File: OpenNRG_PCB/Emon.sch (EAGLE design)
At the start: 63 parts, among them J1 POWER_JACKSMD, Q4 16000, U1 ATMEGA368

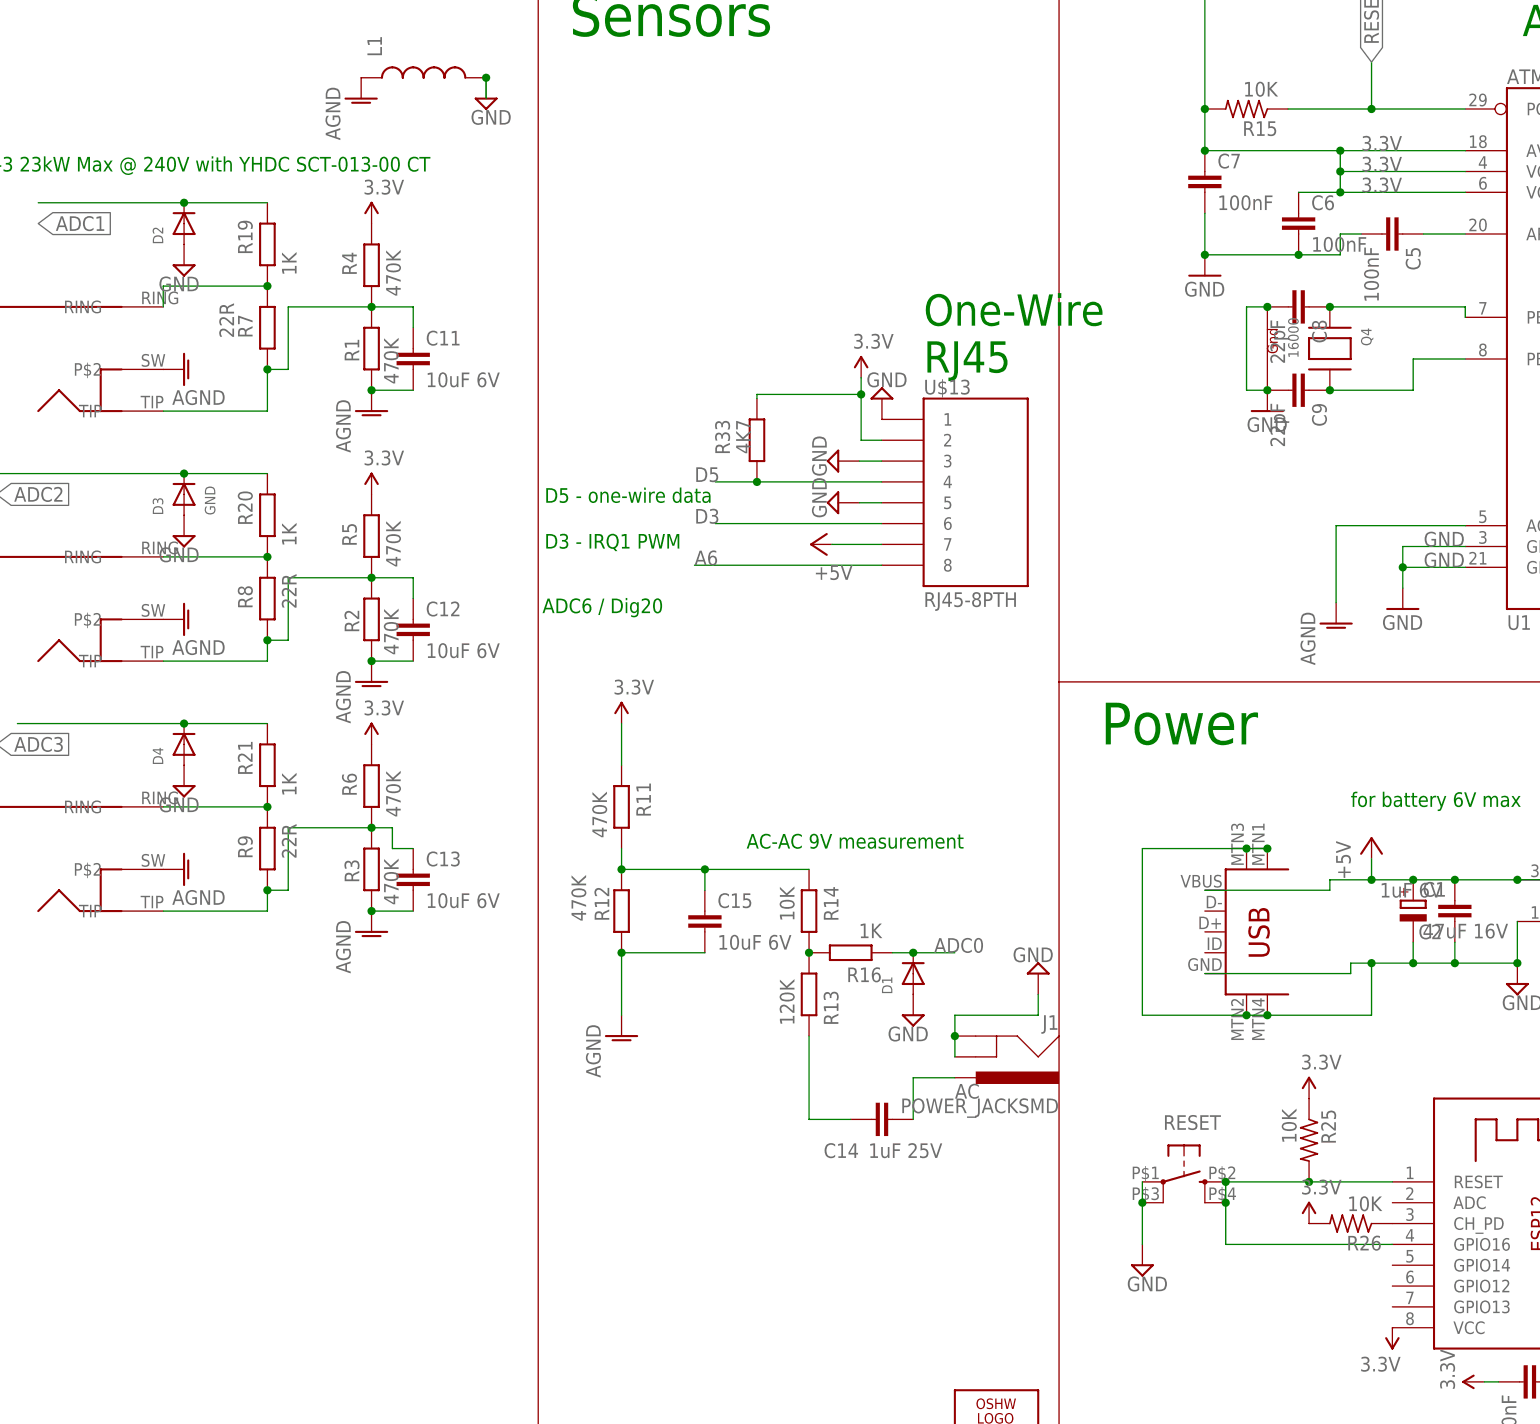
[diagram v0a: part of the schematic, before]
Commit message: Re-write or ESP code and updated to board files
Update to ESP8266 firmware to support latest board manager.
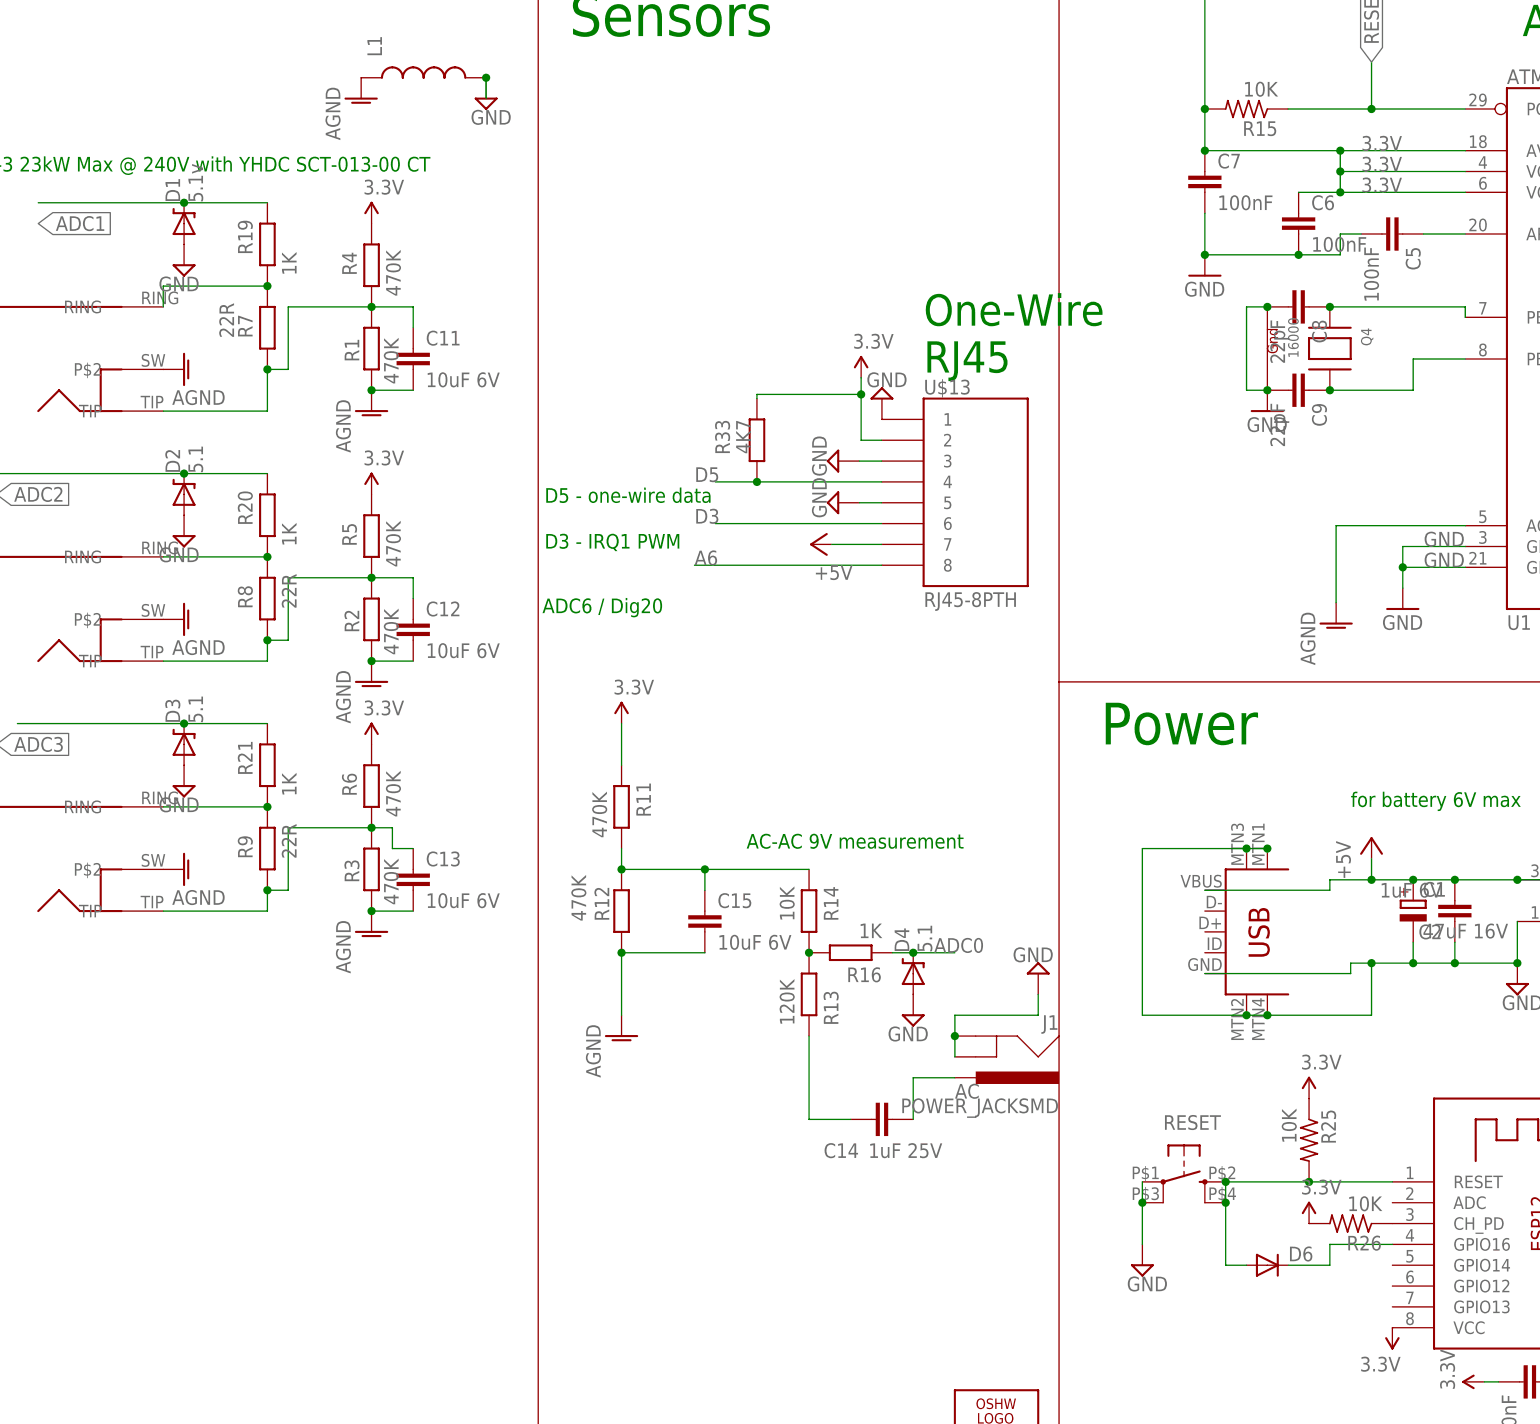
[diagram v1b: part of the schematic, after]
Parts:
- added D6: (no value), SparkFun:DIODESOD
- D1: value (none) -> 5.1v; device microbuilder:DIODESOD-523 -> SparkFun:DIODE-ZENER-BZT52
- D2, D4: value (none) -> 5.1; device microbuilder:DIODESOD-523 -> SparkFun:DIODE-ZENER-BZT52
- D3: value GND -> 5.1; device microbuilder:DIODESOD-523 -> SparkFun:DIODE-ZENER-BZT52
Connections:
- new net N$12: D6.C, X1.GPIO16
- net ADC0: now also D4.C; no longer D1.C
- net ADC1: now also D1.C; no longer D2.C
- net ADC2: now also D2.C; no longer D3.C
- net ADC3: now also D3.C; no longer D4.C
- net N$15: now also D6.A; no longer X1.GPIO16
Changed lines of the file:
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@@
 <part name="P+9" library="supply1" deviceset="+5V" device=""/>
 <part name="AGND11" library="supply1" deviceset="AGND" device=""/>
-<part name="D2" library="microbuilder" deviceset="DIODE" device="SOD-523"/>
-<part name="D3" library="microbuilder" deviceset="DIODE" device="SOD-523" value="GND"/>
-<part name="D4" library="microbuilder" deviceset="DIODE" device="SOD-523"/>
 <part name="SUPPLY14" library="supply2" deviceset="GND" device=""/>
 <part name="SUPPLY16" library="supply2" deviceset="GND" device=""/>
 <part name="SUPPLY17" library="supply2" deviceset="GND" device=""/>
-<part name="D1" library="microbuilder" deviceset="DIODE" device="SOD-523"/>
 <part name="SUPPLY18" library="supply2" deviceset="GND" device=""/>
 <part name="P+2" library="supply1" deviceset="+5V" device=""/>
@@
 <part name="U$3" library="Qxd" deviceset="MJ-3523-SMT" device=""/>
 <part name="J1" library="SparkFun" deviceset="POWER_JACK" device="SMD"/>
-<part name="U$4" library="Qxd" deviceset="AUDIO_SMT" device=""/>
+<part name="D1" library="SparkFun" deviceset="DIODE-ZENER" device="-BZT52" value="5.1v"/>
+<part name="D2" library="SparkFun" deviceset="DIODE-ZENER" device="-BZT52" value="5.1"/>
+<part name="D3" library="SparkFun" deviceset="DIODE-ZENER" device="-BZT52" value="5.1"/>
+<part name="D4" library="SparkFun" deviceset="DIODE-ZENER" device="-BZT52" value="5.1"/>
+<part name="D6" library="SparkFun" deviceset="DIODE" device="SOD"/>
 </parts>
 <sheets>
@@
 <instance part="P+9" gate="1" x="7.874" y="308.864" rot="R90"/>
 <instance part="AGND11" gate="VR1" x="71.882" y="299.212"/>
-<instance part="D2" gate="G$1" x="-68.58" y="347.98" rot="R90"/>
-<instance part="D3" gate="G$1" x="-68.58" y="314.96" rot="R90"/>
-<instance part="D4" gate="G$1" x="-68.58" y="284.48" rot="R90"/>
 <instance part="SUPPLY14" gate="GND" x="-68.58" y="279.4" rot="MR0"/>
 <instance part="SUPPLY16" gate="GND" x="-68.58" y="342.9" rot="MR0"/>
 <instance part="SUPPLY17" gate="GND" x="-68.58" y="309.88" rot="MR0"/>
-<instance part="D1" gate="G$1" x="20.32" y="256.54" rot="R90"/>
 <instance part="SUPPLY18" gate="GND" x="20.32" y="251.46" rot="MR0"/>
 <instance part="P+2" gate="1" x="256.54" y="321.31"/>
@@
 <instance part="U$3" gate="G$1" x="-86.36" y="271.78"/>
 <instance part="J1" gate="G$1" x="27.94" y="251.46" rot="R180"/>
+<instance part="D1" gate="G$1" x="-68.58" y="347.98" rot="R90"/>
+<instance part="D2" gate="G$1" x="-68.58" y="314.96" rot="R90"/>
+<instance part="D3" gate="G$1" x="-68.58" y="284.48" rot="R90"/>
+<instance part="D4" gate="G$1" x="20.32" y="256.54" rot="R90"/>
+<instance part="D6" gate="G$1" x="63.5" y="220.98"/>
 </instances>
 <busses>
@@
 </segment>
 <segment>
-<pinref part="D4" gate="G$1" pin="A"/>
-<pinref part="SUPPLY14" gate="GND" pin="GND"/>
-</segment>
-<segment>
-<pinref part="D2" gate="G$1" pin="A"/>
-<pinref part="SUPPLY16" gate="GND" pin="GND"/>
-</segment>
-<segment>
-<pinref part="D3" gate="G$1" pin="A"/>
-<pinref part="SUPPLY17" gate="GND" pin="GND"/>
-</segment>
-<segment>
-<pinref part="D1" gate="G$1" pin="A"/>
-<pinref part="SUPPLY18" gate="GND" pin="GND"/>
-</segment>
-<segment>
 <pinref part="X1" gate="G$1" pin="GND"/>
 <pinref part="SUPPLY4" gate="GND" pin="GND"/>
@@
 <wire x1="218.44" y1="261.62" x2="226.06" y2="261.62" width="0.1524" layer="91"/>
 </segment>
+<segment>
+<pinref part="SUPPLY16" gate="GND" pin="GND"/>
+<pinref part="D1" gate="G$1" pin="A"/>
+</segment>
+<segment>
+<pinref part="SUPPLY17" gate="GND" pin="GND"/>
+<pinref part="D2" gate="G$1" pin="A"/>
+</segment>
+<segment>
+<pinref part="SUPPLY14" gate="GND" pin="GND"/>
+<pinref part="D3" gate="G$1" pin="A"/>
+</segment>
+<segment>
+<pinref part="SUPPLY18" gate="GND" pin="GND"/>
+<pinref part="D4" gate="G$1" pin="A"/>
+</segment>
 </net>
 <net name="ADC0" class="0">
 <segment>
 <pinref part="R16" gate="G$1" pin="1"/>
+<label x="22.86" y="259.08" size="1.778" layer="95"/>
 <wire x1="17.78" y1="259.08" x2="20.32" y2="259.08" width="0.1524" layer="91"/>
-<label x="22.86" y="259.08" size="1.778" layer="95"/>
-<pinref part="D1" gate="G$1" pin="C"/>
+<pinref part="D4" gate="G$1" pin="C"/>
 <wire x1="20.32" y1="259.08" x2="25.4" y2="259.08" width="0.1524" layer="91"/>
 <junction x="20.32" y="259.08"/>
@@
 <segment>
 <label x="-86.36" y="347.98" size="1.778" layer="95" xref="yes"/>
-<pinref part="D2" gate="G$1" pin="C"/>
 <pinref part="R19" gate="G$1" pin="2"/>
+<wire x1="-86.36" y1="350.52" x2="-68.58" y2="350.52" width="0.1524" layer="91"/>
+<pinref part="D1" gate="G$1" pin="C"/>
 <wire x1="-68.58" y1="350.52" x2="-58.42" y2="350.52" width="0.1524" layer="91"/>
-<wire x1="-86.36" y1="350.52" x2="-68.58" y2="350.52" width="0.1524" layer="91"/>
 <junction x="-68.58" y="350.52"/>
 </segment>
@@
 </segment>
 <segment>
+<wire x1="-58.42" y1="317.5" x2="-68.58" y2="317.5" width="0.1524" layer="91"/>
+<label x="-91.44" y="314.96" size="1.778" layer="95" xref="yes"/>
+<pinref part="R20" gate="G$1" pin="2"/>
+<pinref part="D2" gate="G$1" pin="C"/>
 <wire x1="-68.58" y1="317.5" x2="-91.44" y2="317.5" width="0.1524" layer="91"/>
-<label x="-91.44" y="314.96" size="1.778" layer="95" xref="yes"/>
-<pinref part="D3" gate="G$1" pin="C"/>
-<pinref part="R20" gate="G$1" pin="2"/>
-<wire x1="-68.58" y1="317.5" x2="-58.42" y2="317.5" width="0.1524" layer="91"/>
 <junction x="-68.58" y="317.5"/>
 </segment>
@@
 <segment>
 <label x="-91.44" y="284.48" size="1.778" layer="95" xref="yes"/>
-<pinref part="D4" gate="G$1" pin="C"/>
 <pinref part="R21" gate="G$1" pin="2"/>
+<wire x1="-88.9" y1="287.02" x2="-68.58" y2="287.02" width="0.1524" layer="91"/>
+<pinref part="D3" gate="G$1" pin="C"/>
 <wire x1="-68.58" y1="287.02" x2="-58.42" y2="287.02" width="0.1524" layer="91"/>
-<wire x1="-88.9" y1="287.02" x2="-68.58" y2="287.02" width="0.1524" layer="91"/>
 <junction x="-68.58" y="287.02"/>
 </segment>
@@
 <wire x1="68.58" y1="231.14" x2="78.74" y2="231.14" width="0.1524" layer="91"/>
 <junction x="68.58" y="231.14"/>
-<pinref part="X1" gate="G$1" pin="GPIO16"/>
-<wire x1="78.74" y1="223.52" x2="58.42" y2="223.52" width="0.1524" layer="91"/>
-<wire x1="58.42" y1="223.52" x2="58.42" y2="228.6" width="0.1524" layer="91"/>
+<wire x1="58.42" y1="220.98" x2="58.42" y2="228.6" width="0.1524" layer="91"/>
 <junction x="58.42" y="228.6"/>
+<wire x1="58.42" y1="220.98" x2="60.96" y2="220.98" width="0.1524" layer="91"/>
+<pinref part="D6" gate="G$1" pin="A"/>
 </segment>
 </net>
@@
 </segment>
 </net>
+<net name="N$12" class="0">
+<segment>
+<wire x1="66.04" y1="220.98" x2="71.12" y2="220.98" width="0.1524" layer="91"/>
+<wire x1="71.12" y1="220.98" x2="71.12" y2="223.52" width="0.1524" layer="91"/>
+<pinref part="X1" gate="G$1" pin="GPIO16"/>
+<wire x1="71.12" y1="223.52" x2="78.74" y2="223.52" width="0.1524" layer="91"/>
+<pinref part="D6" gate="G$1" pin="C"/>
+</segment>
+</net>
